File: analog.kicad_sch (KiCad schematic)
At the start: 30 parts, among them J6 Conn_01x02_Pin, U3 TL082, U4 LM358

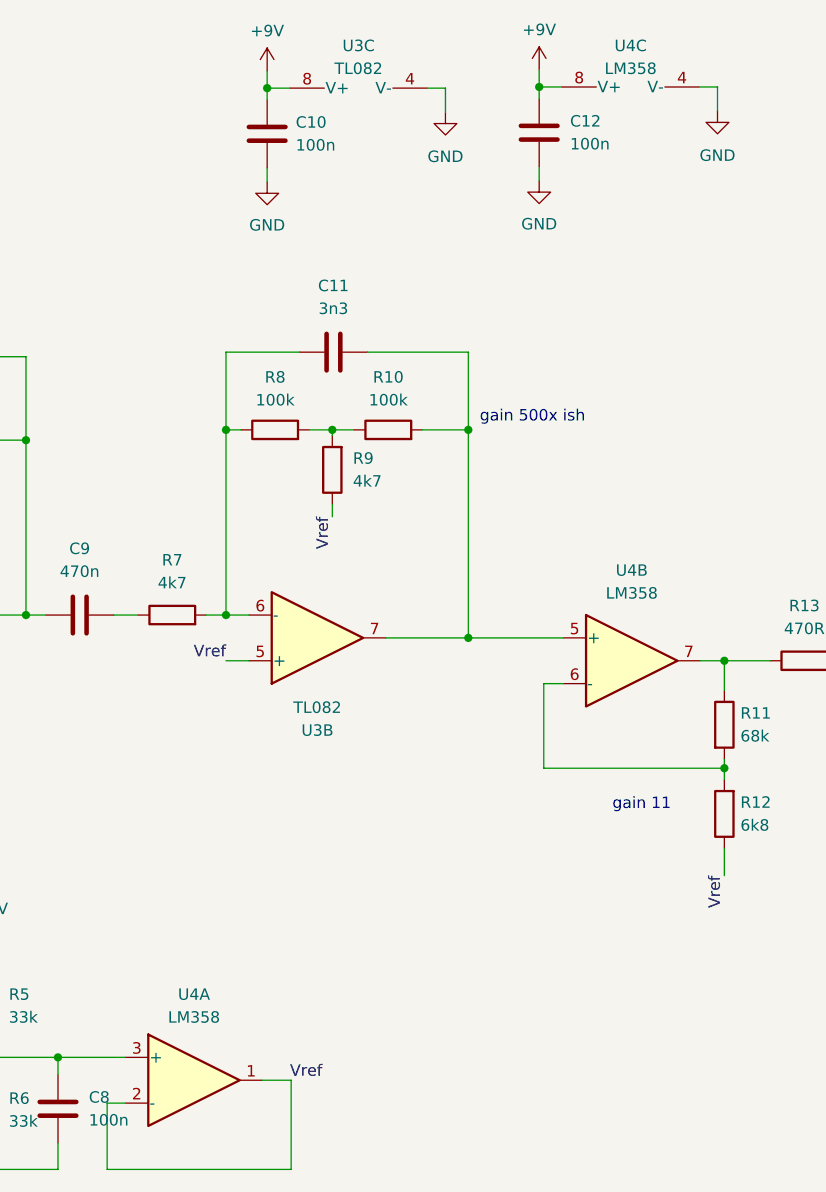
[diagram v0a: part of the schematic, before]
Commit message: op amp type update, lm358->tl082, bulk purchase=cheaper, higher badwidth, still super cheap
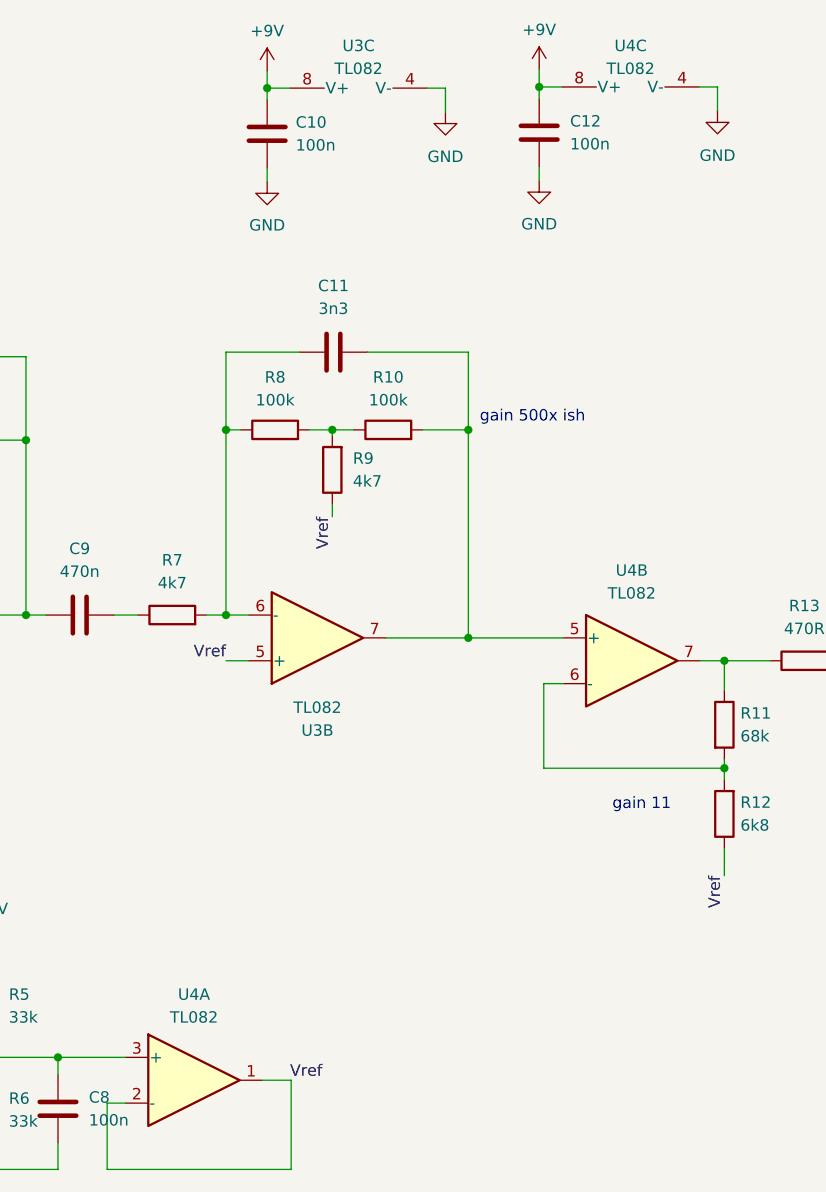
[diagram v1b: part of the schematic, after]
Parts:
- U4: value LM358 -> TL082
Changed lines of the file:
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@@
       (effects (font (size 1.27 1.27)))
     )
-    (property "Value" "LM358" (at 197.358 88.773 0)
+    (property "Value" "TL082" (at 197.358 88.773 0)
       (effects (font (size 1.27 1.27)))
     )
@@
       (effects (font (size 1.27 1.27)) hide)
     )
-    (property "Datasheet" "http://www.ti.com/lit/ds/symlink/lm2904-n.pdf" (at 197.358 96.266 0)
+    (property "Datasheet" "" (at 197.358 96.266 0)
       (effects (font (size 1.27 1.27)) hide)
     )
@@
       (effects (font (size 1.27 1.27)))
     )
-    (property "Value" "LM358" (at 197.231 30.48 90)
+    (property "Value" "TL082" (at 197.231 30.48 90)
       (effects (font (size 1.27 1.27)))
     )
@@
       (effects (font (size 1.27 1.27)) hide)
     )
-    (property "Datasheet" "http://www.ti.com/lit/ds/symlink/lm2904-n.pdf" (at 197.231 29.972 0)
+    (property "Datasheet" "" (at 197.231 29.972 0)
       (effects (font (size 1.27 1.27)) hide)
     )
@@
       (effects (font (size 1.27 1.27)))
     )
-    (property "Value" "LM358" (at 148.717 135.89 0)
+    (property "Value" "TL082" (at 148.717 135.89 0)
       (effects (font (size 1.27 1.27)))
     )
@@
       (effects (font (size 1.27 1.27)) hide)
     )
-    (property "Datasheet" "http://www.ti.com/lit/ds/symlink/lm2904-n.pdf" (at 148.717 142.875 0)
-      (effects (font (size 1.27 1.27)) hide)
-    )
+    (property "Datasheet" "" (at 148.717 142.875 0)
+      (effects (font (size 1.27 1.27)) hide)
+    )
